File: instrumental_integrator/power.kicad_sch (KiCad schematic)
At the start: 15 parts, among them J1 SS-52400-003, U8 LM27762

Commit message: added footprint links and changed instr opamp to ina828
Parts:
- removed J1: SS-52400-003, footprintsesp32:BELFUSE_SS-52400-003, symbol symesp32:SS-52400-003
- added J2: SS-52400-003, SS-52400-003:BELFUSE_SS-52400-003, symbol SS-52400-003:SS-52400-003
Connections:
- net GND: now also J2.A1 (GNDA1), J2.A12 (GNDA2), J2.B1 (GNDB1), J2.B12 (GNDB2), J2.G1 (GND/SHIELD), J2.G2 (GND/SHIELD), J2.G3 (GND/SHIELD), J2.G4 (GND/SHIELD), J2.S1 (GND/SHIELD), J2.S2 (GND/SHIELD), J2.S3 (GND/SHIELD), J2.S4 (GND/SHIELD)
- net VBUS: now also J2.A4 (VBUSA1), J2.A9 (VBUSA2), J2.B4 (VBUSB1), J2.B9 (VBUSB2)
- net at R19.1: now also J2.A5 (CC1)
- net at R20.1: now also J2.B5 (CC2)

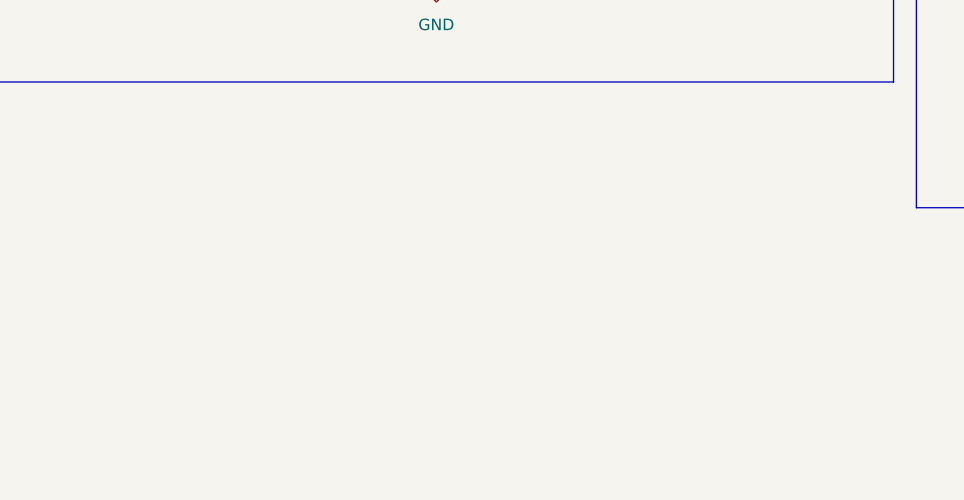
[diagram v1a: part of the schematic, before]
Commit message: added testpoints adn +- 15V rails and resistor chain asw from previous iteration
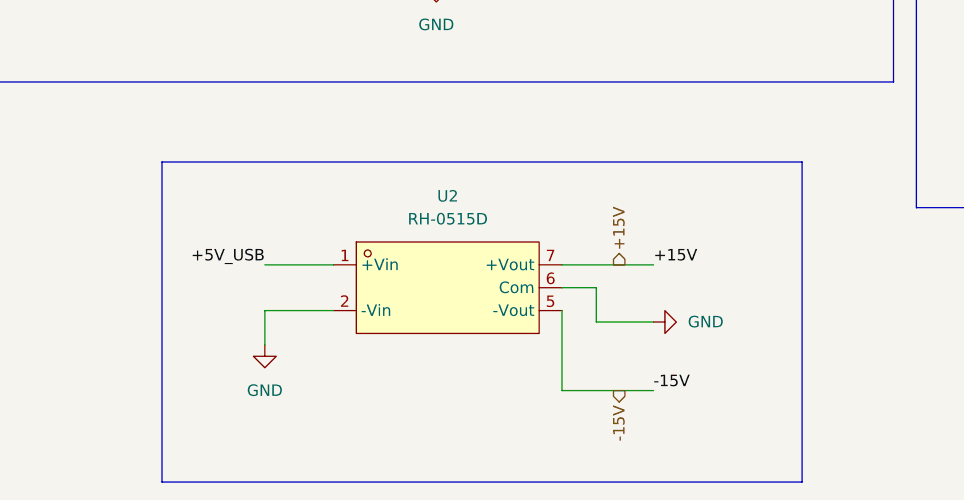
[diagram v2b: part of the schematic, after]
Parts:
- added U2: RH-0515D, easyeda2kicad:PWRM-TH_5P-L19.7-W6.0-P2.54_RH-051509D, symbol easyeda2kicad:RH-0515D
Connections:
- net +5V: now also U2.1 (+Vin)
- net GND: now also U2.2 (-Vin), U2.6 (Com)
- new net +15V: U2.7 (+Vout)
- new net -15V: U2.5 (-Vout)

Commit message: switch footprints v2
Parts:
- U2: Manufacturer YLPTEC(易川) -> (none)

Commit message: added stuff, removedf some stuff
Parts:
- removed U2: RH-0515D, easyeda2kicad:PWRM-TH_5P-L19.7-W6.0-P2.54_RH-051509D, symbol easyeda2kicad:RH-0515D
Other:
- moved on the sheet: C23, F1, J2, R19, R20

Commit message: started pcb
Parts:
- removed C23: 0.1u, symbol Device:C
- removed F1: 0ZCH0110AF2E, 0ZCH0110AF2E:FUSC3225X100N, symbol 0ZCH0110AF2E:0ZCH0110AF2E
- removed J2: SS-52400-003, SS-52400-003:BELFUSE_SS-52400-003, symbol SS-52400-003:SS-52400-003
- removed R19, R20: 5.1k, symbol Device:R
- added C26: 0.1u, Capacitor_SMD:C_0805_2012Metric, symbol Device:C
- added F1: 0ZCH0110AF2E, easyeda2kicad:F1210, symbol easyeda2kicad:0ZCH0110AF2E
- added R26, R31: 5.1k, Resistor_SMD:R_0805_2012Metric, symbol Device:R
- added USB1: SS-52400-003, easyeda2kicad:TYPE-C-SMD_SS-52400-003, symbol easyeda2kicad:SS-52400-003
- C18, C19: value C -> 2.2u; footprint (none) -> Capacitor_SMD:C_0805_2012Metric
- C20, C21, C22: footprint (none) -> Capacitor_SMD:C_0805_2012Metric
- R15, R16, R17, R18: footprint (none) -> Resistor_SMD:R_0805_2012Metric
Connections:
- net +5V: now also F1.1
- net GND: now also C26.2, R26.2, R31.2, USB1.A1 (GND), USB1.A12 (GND), USB1.B1 (GND), USB1.B12 (GND), USB1.GND
- net VBUS: now also C26.1, F1.2, USB1.A4 (VBUS), USB1.A9 (VBUS), USB1.B4 (VBUS), USB1.B9 (VBUS)
- new net: R26.1, USB1.B5 (CC2)
- new net: R31.1, USB1.A5 (CC1)
- no-connect marks 15 -> 18
